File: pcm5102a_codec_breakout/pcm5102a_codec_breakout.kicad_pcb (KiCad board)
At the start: 2 copper layers, 40 x 20 mm, 13 parts, among them J101 Conn_01x07_Female, J102 AudioJack3, U101 pcm5102a

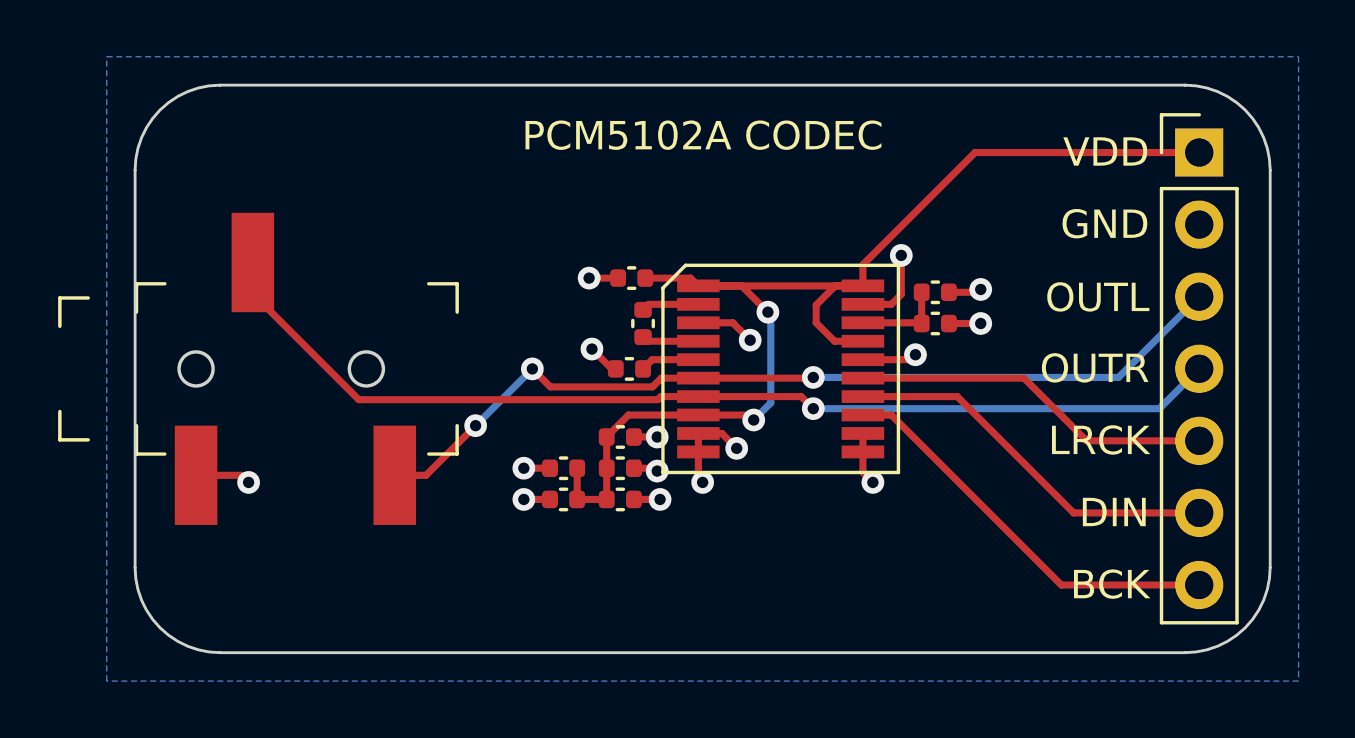
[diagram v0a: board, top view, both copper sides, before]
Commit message: [pcm5102a_codec_breakout] Schematic fixes and re-routing
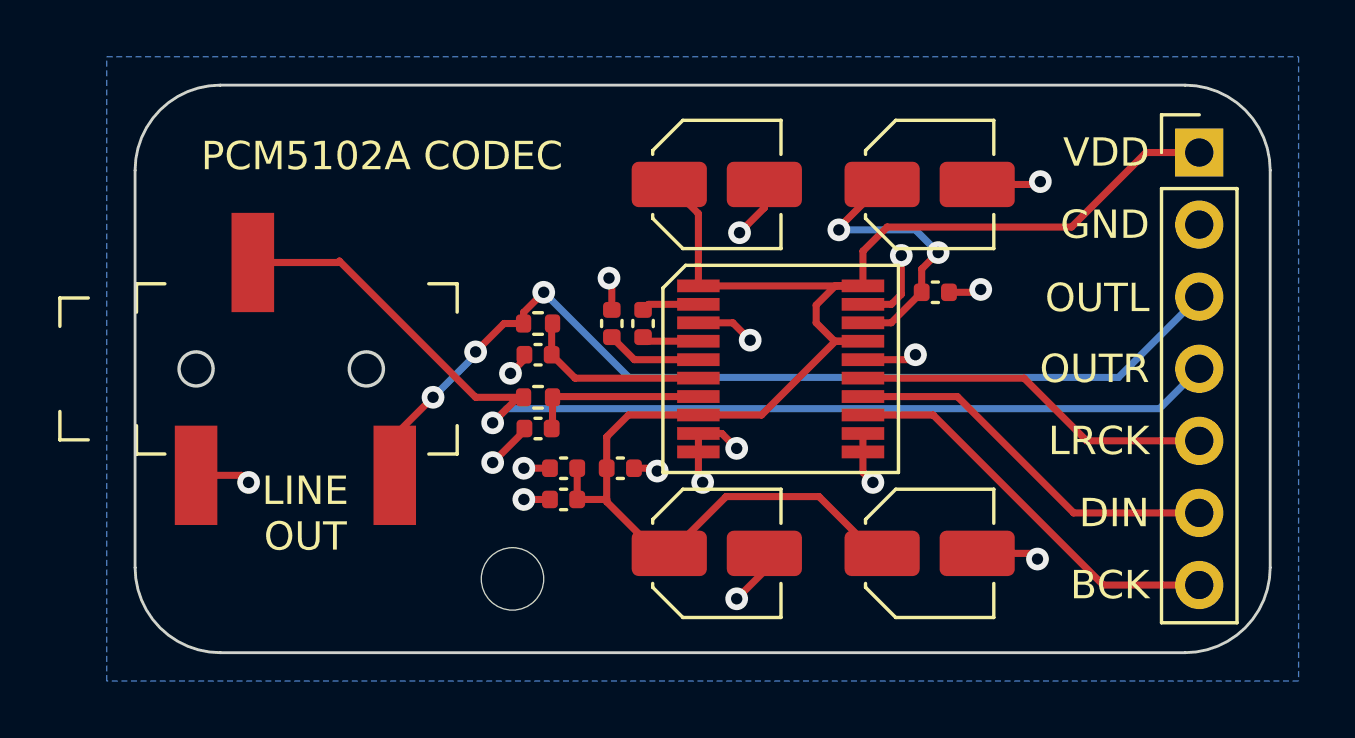
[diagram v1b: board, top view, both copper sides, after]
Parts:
- added C111: 2.2n, Capacitor_SMD:C_0402_1005Metric, F.Cu at (134.2, 89.5)
- added C112: 2.2n, Capacitor_SMD:C_0402_1005Metric, F.Cu at (134.2, 92.1)
- added R101: 470, Resistor_SMD:R_0402_1005Metric, F.Cu at (134.2, 88.4)
- added R102: 470, Resistor_SMD:R_0402_1005Metric, F.Cu at (134.2, 91.0)
- added REF**: MountingHole_2.2mm_M2, MountingHole:MountingHole_2.2mm_M2, F.Cu at (133.3, 97.4)
- C102, C105, C109, C110: footprint Capacitor_SMD:C_0402_1005Metric -> Capacitor_SMD:C_Elec_4x5.4
- moved C109 11.6 mm to (148.0, 96.5)
- moved C110 4.90 mm to (148.0, 83.5)
- moved C102 4.46 mm to (140.5, 83.5), turned to 0 degrees
- moved C105 3.89 mm to (140.5, 96.5)
- moved C104 1.72 mm to (136.8, 88.4), turned to -90 degrees
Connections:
- U101 pad 6: OUTL -> Net-(U101-Pad6)
- U101 pad 7: OUTR -> Net-(U101-Pad7)
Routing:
- net VDD: track 43.3 -> 55.4 mm, vias 2 -> 0
- net GND: track 23.0 -> 30.2 mm, vias 16 -> 18
- net Net-(C108-Pad2): track 3.18 -> 10.2 mm, vias 0 -> 2
- net Net-(U101-Pad6): track 0.00 -> 6.62 mm
- net Net-(U101-Pad7): track 0.00 -> 6.26 mm
- net OUTL: track 31.6 -> 34.5 mm
- net OUTR: track 36.8 -> 38.7 mm
- net Net-(C104-Pad2): track 2.08 -> 3.38 mm
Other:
- board text added: "LINE OUT"
- board text added: "V1"

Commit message: [pcm5102a_codec_breakout] Tweaks and fixes
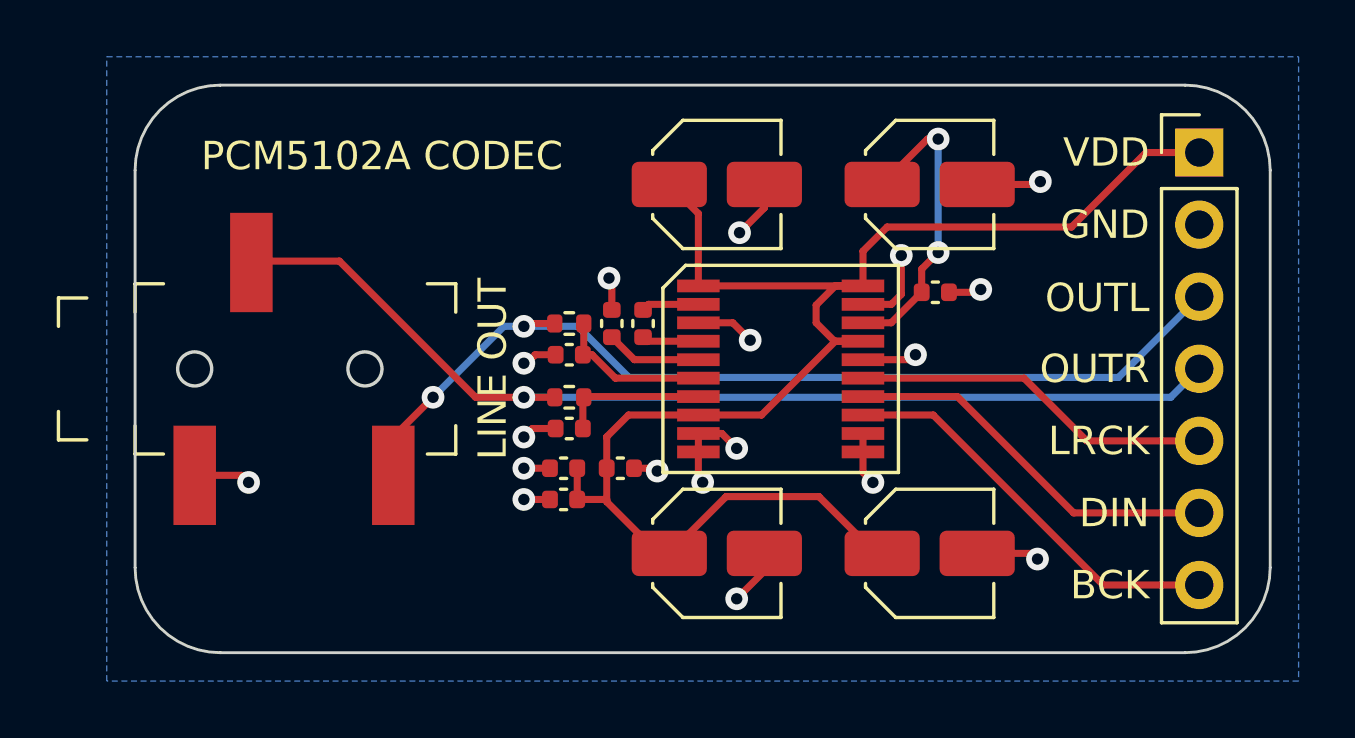
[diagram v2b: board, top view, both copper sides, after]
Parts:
- removed REF**: MountingHole_2.2mm_M2, MountingHole:MountingHole_2.2mm_M2
- moved C111 1.10 mm to (135.3, 89.5)
- moved C112 1.10 mm to (135.3, 92.1)
- moved R101 1.10 mm to (135.3, 88.4)
- moved R102 1.10 mm to (135.3, 91.0)
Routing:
- net OUTR: track 38.7 -> 36.7 mm
- net Net-(C111-Pad1): track 6.62 -> 5.52 mm
- net Net-(C112-Pad2): track 6.26 -> 5.16 mm
- net Net-(C108-Pad2): track 10.2 -> 10.8 mm
- net OUTL: track 34.5 -> 34.4 mm, vias 3 -> 2

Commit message: [pcm5102a_codec_breakout] V1 JLCPCB fab files
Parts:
- added REF**: MountingHole_2.1mm, MountingHole:MountingHole_2.1mm, F.Cu at (132.1, 97.4)
- added REF**: MountingHole_2.1mm, MountingHole:MountingHole_2.1mm, F.Cu at (132.1, 84.4)
- moved C111 1.50 mm to (135.3, 88.0), turned to 0 degrees
- moved R101 0.60 mm to (135.3, 89.0)
- turned C112 to 180 degrees
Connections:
- C111 pad 1: Net-(C111-Pad1) -> OUTL
- C112 pad 2: Net-(C112-Pad2) -> OUTR
- R101 pad 2: Net-(C111-Pad1) -> Net-(R101-Pad2)
- R102 pad 2: Net-(C112-Pad2) -> Net-(R102-Pad2)
- U101 pad 6: Net-(C111-Pad1) -> Net-(R101-Pad2)
- U101 pad 7: Net-(C112-Pad2) -> Net-(R102-Pad2)
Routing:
- net Net-(C111-Pad1): track 5.52 -> 0.00 mm
- net Net-(C112-Pad2): track 5.16 -> 0.00 mm
- net Net-(R101-Pad2): track 0.00 -> 4.59 mm
- net Net-(R102-Pad2): track 0.00 -> 4.05 mm
- net OUTR: track 36.7 -> 37.9 mm
- net OUTL: track 34.4 -> 35.6 mm
